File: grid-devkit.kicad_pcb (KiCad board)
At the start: 4 copper layers, 32.7 x 99.7 mm, 167 parts, among them J601 TYPE-C-32-M-12, J603 Conn_01x04, J604 Conn_01x04, J605 Conn_01x03, J610 Conn_01x08, J611 Conn_01x08, J701 C5137195, J702 Conn_02x05_Odd_Even, SW609 model_code, SW610 rev_code, SW701 C255807, SW702 C2905169, SW703 C2905169, U1001 74HC4051, U1002 74HC4051, U601 LN1134A332MR-G, U602 C5451661, U603 C5451661, U604 74LVC1G08, U605 BL1551B, U606 BL1551B, U607 BL1551B, U608 BL1551B, U609 74HC165, U610 APS1604M-3SQR-ZR, U703 RP2040, U704 ESP32-S3, U705 W25Q64JVSSIQ, U801 74HC165, U903 APS1604M-3SQR-SN, U918 NS4168_C910588, Y701 40MHz

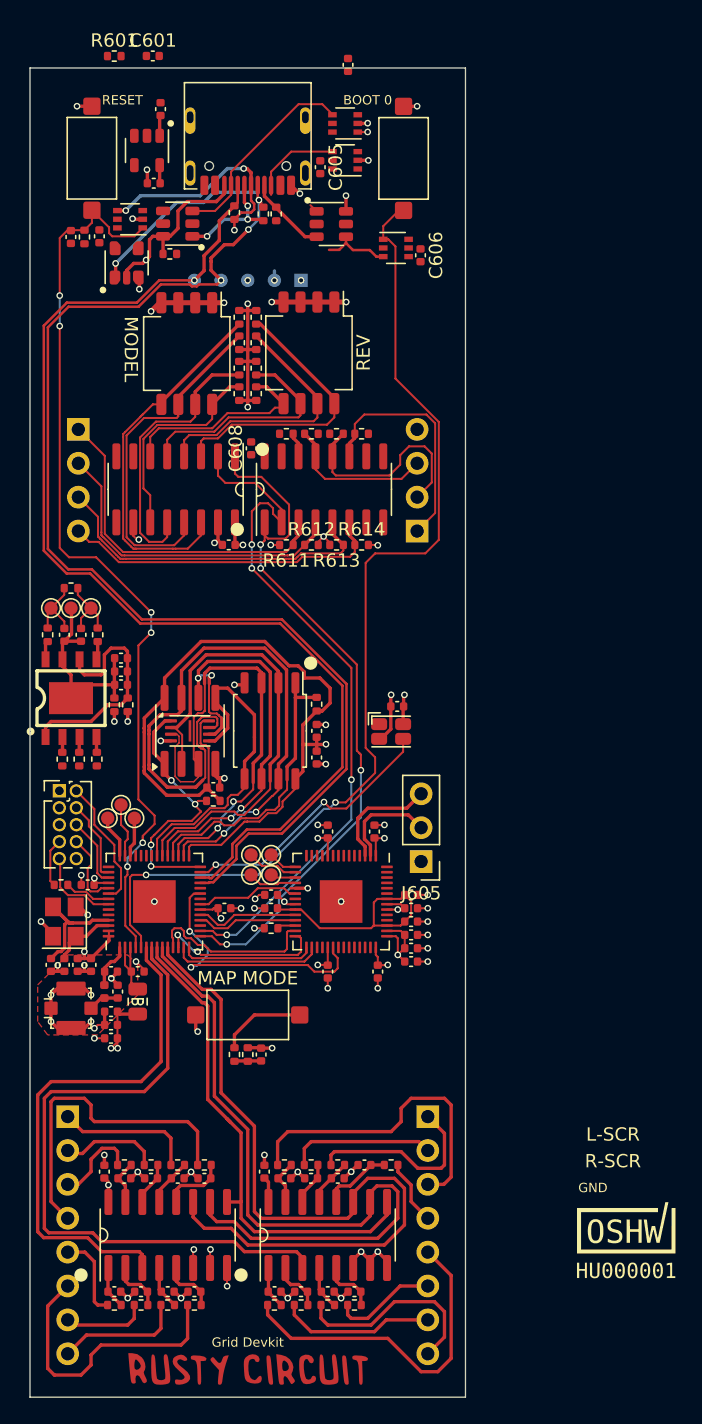
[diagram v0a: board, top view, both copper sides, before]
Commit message: Adds traces
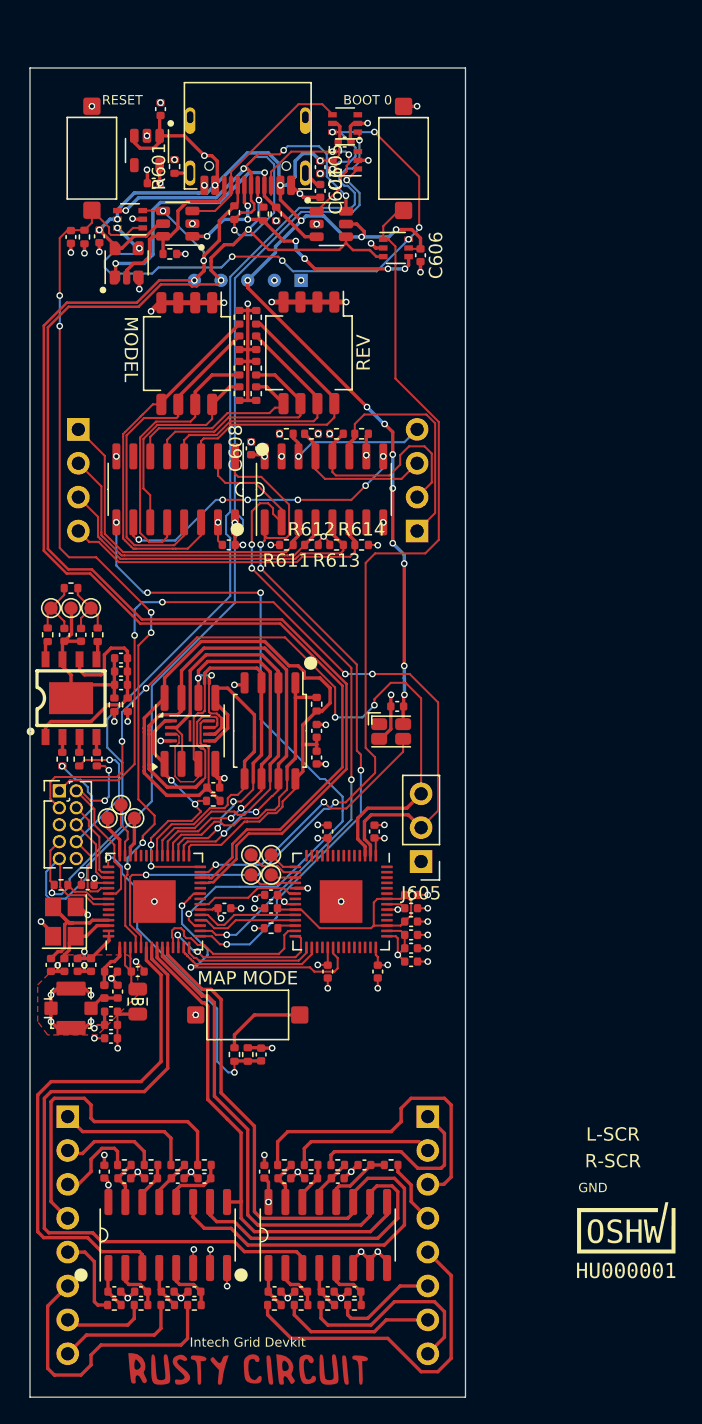
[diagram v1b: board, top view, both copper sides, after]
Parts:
- moved C601 16.1 mm to (105.4, 56.7), turned to -90 degrees
- moved R601 9.43 mm to (94.5, 54.9), turned to 90 degrees
- moved C604 5.80 mm to (107.3, 53.1), turned to 0 degrees
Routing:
- net +5V: track 3.79 -> 107.8 mm, vias 2 -> 18
- net ESP_GPIO_44: track 6.33 -> 78.4 mm, vias 0 -> 1
- net ESP_GPIO_43: track 4.39 -> 76.4 mm, vias 1 -> 2
- net /MCU/RP_UART0_TX: track 7.60 -> 61.7 mm, vias 0 -> 4
- net /HWCFG/HWCFG_DATA: track 0.00 -> 50.7 mm, vias 0 -> 4
- net /MCU/RP_UART0_RX: track 8.55 -> 58.5 mm, vias 0 -> 4
- net /MCU/USB_POWER/DEBUG: track 0.00 -> 48.6 mm, vias 0 -> 9
- net /MCU/MAP_MODE: track 1.97 -> 24.0 mm, vias 0 -> 2
- net /LCDBUTTON/DATA: track 1.54 -> 23.0 mm, vias 1 -> 6
- net /MCU/USB_POWER/A6: track 18.1 -> 39.4 mm, vias 4 -> 5
- net /MCU/USB_POWER/A7: track 8.75 -> 22.3 mm, vias 3 -> 7
- net ESP_GPIO_41: track 5.83 -> 16.3 mm, vias 0 -> 1
- net /LCDBUTTON/D3: track 1.86 -> 11.6 mm, vias 0 -> 1
- net /MCU/USB_DN: track 94.4 -> 101.1 mm
- net /MCU/USB_DP: track 85.5 -> 92.0 mm, vias 1 -> 3
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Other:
- board text added: "Intech Grid Devkit"
- board text removed: "Grid Devkit"

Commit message: Updates F.Silkscreen
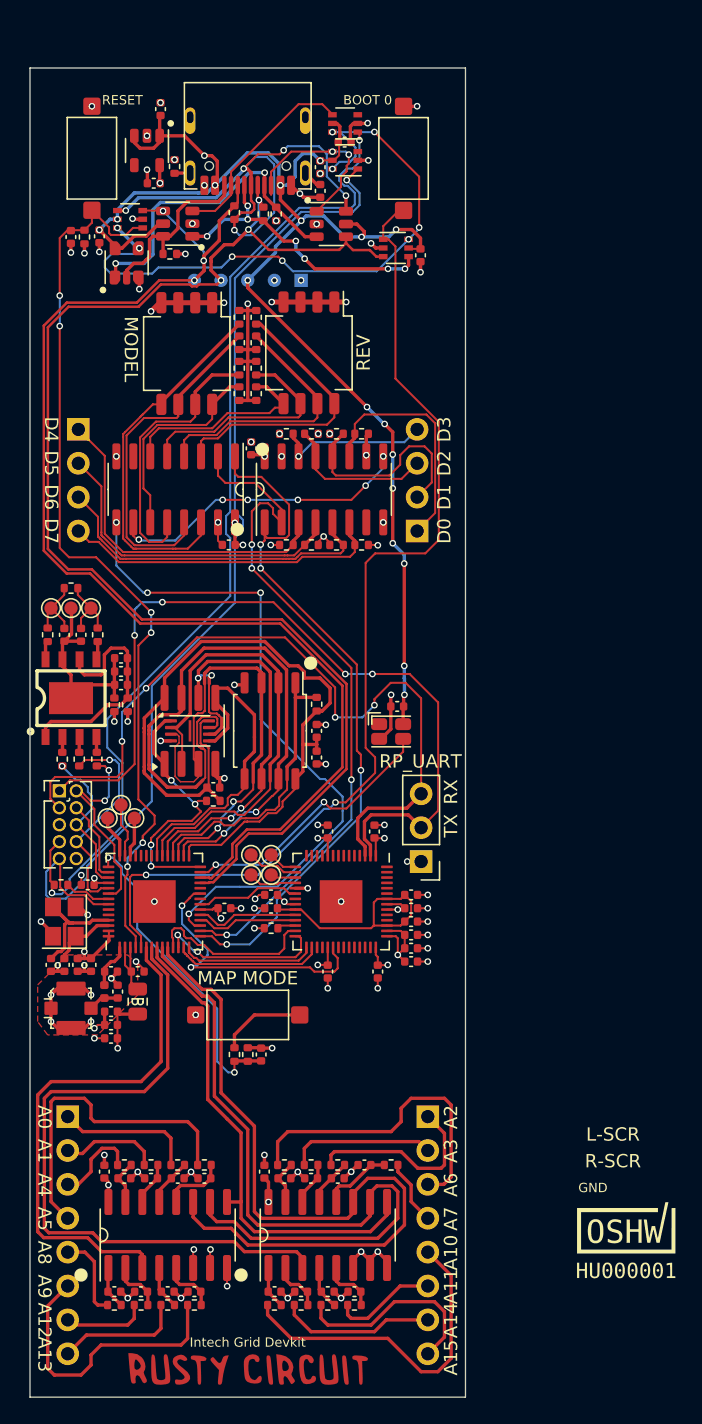
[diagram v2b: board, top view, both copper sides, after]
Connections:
- net /Sheet5D7C8BFD/IN_3 renamed /ANA_5
- net /sheet5D8763D6/IN_3 renamed /ANA_7
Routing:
- net GND: track 92.5 -> 93.5 mm, vias 80 -> 81
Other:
- board text added: "A0"
- board text added: "A1"
- board text added: "A10"
- board text added: "A11"
- board text added: "A12"
- board text added: "A13"
- board text added: "A14"
- board text added: "A15"
- board text added: "A2"
- board text added: "A3"
- board text added: "A4"
- board text added: "A5"
- board text added: "A6"
- board text added: "A7"
- board text added: "A8"
- board text added: "A9"
- board text added: "D0"
- board text added: "D1"
- board text added: "D2"
- board text added: "D3"
- board text added: "D4"
- board text added: "D5"
- board text added: "D6"
- board text added: "D7"
- board text added: "RP_UART"
- board text added: "RX"
- board text added: "TX"
